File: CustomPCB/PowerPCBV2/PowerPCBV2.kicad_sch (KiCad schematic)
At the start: 18 parts, among them J1 XT30, J2 XT60, J3 Barrel_Jack_12V, J4 Barrel_Jack_5V, U1 LM2677T-Fixed-12V, U2 LM2677T-Fixed-5V

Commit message: updates
#23 #20
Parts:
- removed D1, D2: D_Schottky, symbol Device:D_Schottky
- added D1, D2: MBR745, Package_TO_SOT_THT:TO-220-2_Vertical, symbol Diode:MBR745
- CB1, CB2: footprint (none) -> Capacitor_SMD:C_0805_2012Metric_Pad1.18x1.45mm_HandSolder
- Cin1: footprint (none) -> Capacitor_THT:CP_Radial_D16.0mm_P7.50mm
- Cin2: footprint (none) -> Capacitor_THT:CP_Radial_D18.0mm_P7.50mm
- Cout1, Cout2: footprint (none) -> Capacitor_THT:CP_Radial_D10.0mm_P5.00mm
- J3, J4: footprint Connector_BarrelJack:BarrelJack_CUI_PJ-102AH_Horizontal -> Connector_BarrelJack:BarrelJack_CUI_PJ-102AH_Horizontal_flat_pins
- L1, L2: footprint (none) -> Inductor_SMD:MGV1205-1207
- Sin1, Sout1: footprint (none) -> Connector_PinHeader_2.54mm:PinHeader_1x03_P2.54mm_Horizontal
- U1, U2: footprint TO127P457X1016X2052-7P -> LM2677T-ADJ:TO127P457X1016X2052-7P
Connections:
- net GND: now also D1.2 (A), D2.2 (A)
- net at CB2.2, L2.1, U2.1 (SW): now also D2.1 (K)
- net at CB1.2, L1.1, U1.1 (SW): now also D1.1 (K)

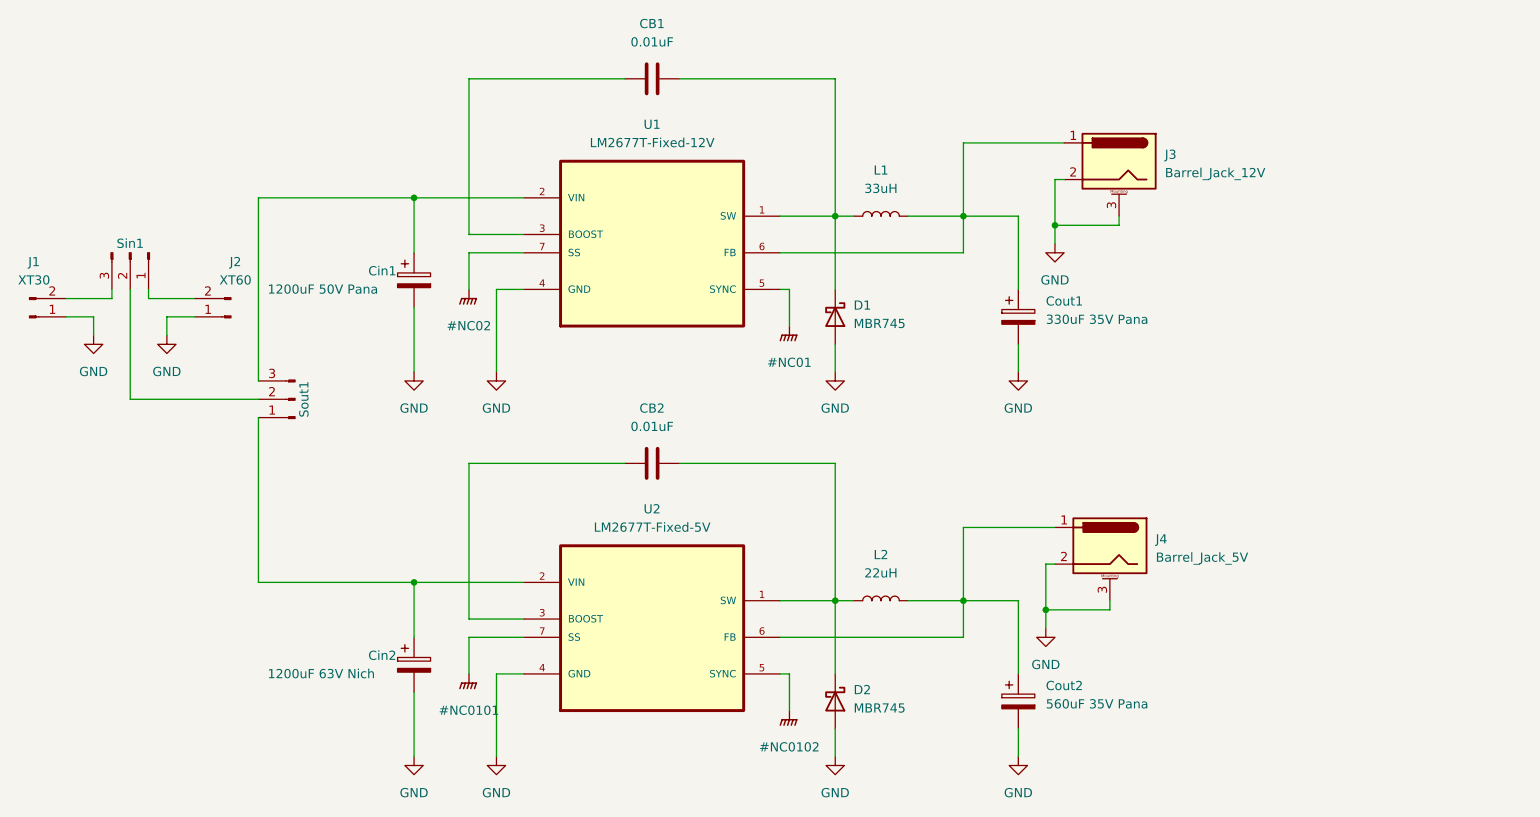
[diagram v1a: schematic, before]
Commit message: update custom pcb and documentation
#23
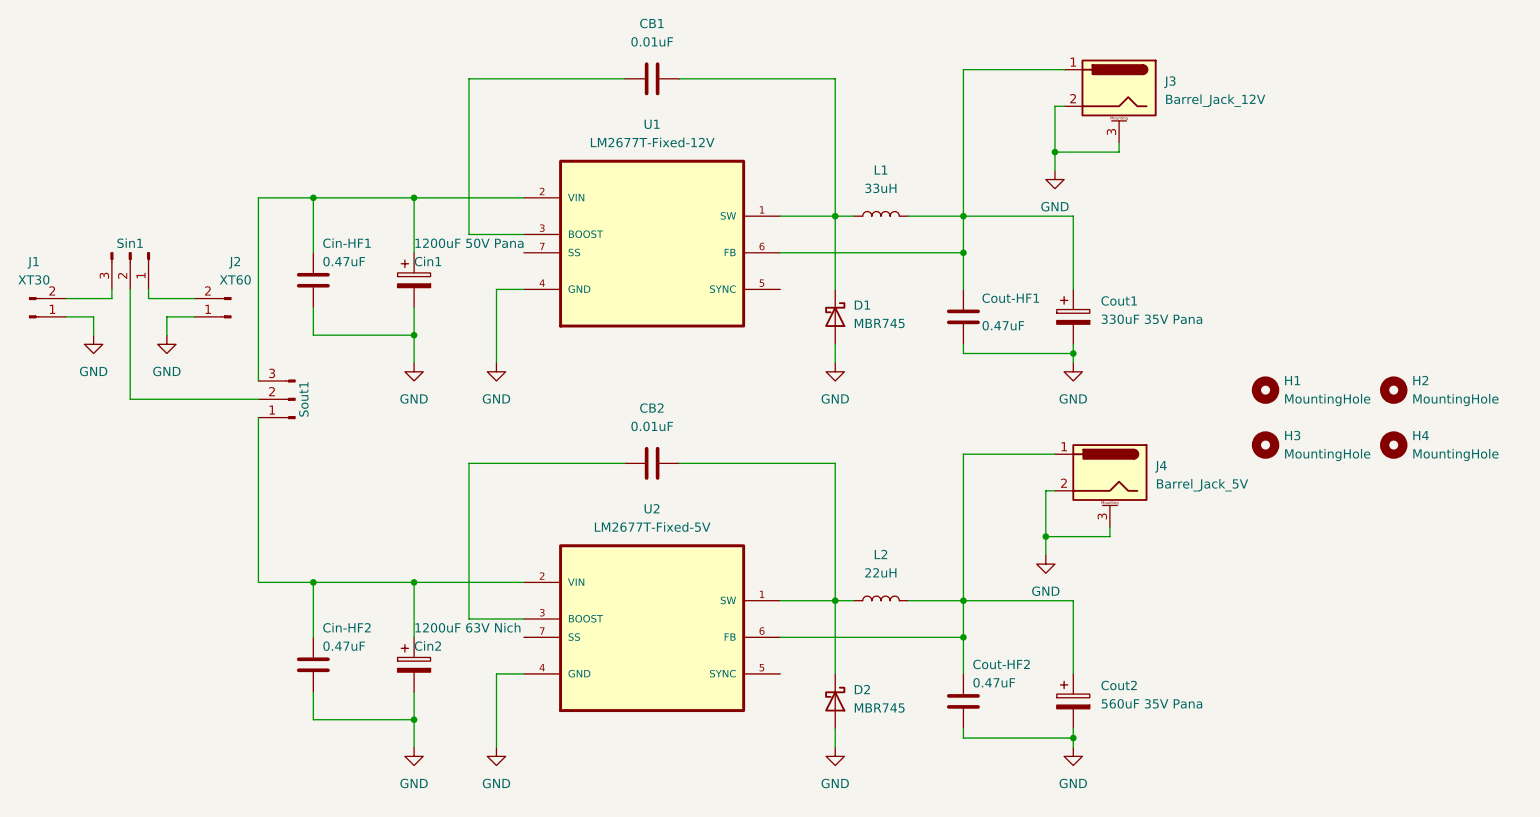
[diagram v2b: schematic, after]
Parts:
- added Cin-HF1, Cin-HF2, Cout-HF1, Cout-HF2: 0.47uF, Capacitor_SMD:C_0805_2012Metric_Pad1.18x1.45mm_HandSolder, symbol Device:C
- added H1, H2, H3, H4: MountingHole, MountingHole:MountingHole_2.5mm, symbol Mechanical:MountingHole
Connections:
- net GND: now also Cin-HF1.2, Cin-HF2.2, Cout-HF1.2, Cout-HF2.2
- net at Cin2.1, Sout1.1 (Pin_1), U2.2 (VIN): now also Cin-HF2.1
- net at Cin1.1, Sout1.3 (Pin_3), U1.2 (VIN): now also Cin-HF1.1
- net at Cout2.1, J4.1, L2.2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: now also Cout-HF2.1
- net at Cout1.1, J3.1, L1.2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: now also Cout-HF1.1
- removed net GNDPWR: U1.5 (SYNC), U1.7 (SS), U2.5 (SYNC), U2.7 (SS)
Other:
- moved on the sheet: Cout1, Cout2, J3, J4
